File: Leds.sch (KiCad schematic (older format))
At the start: 140 parts

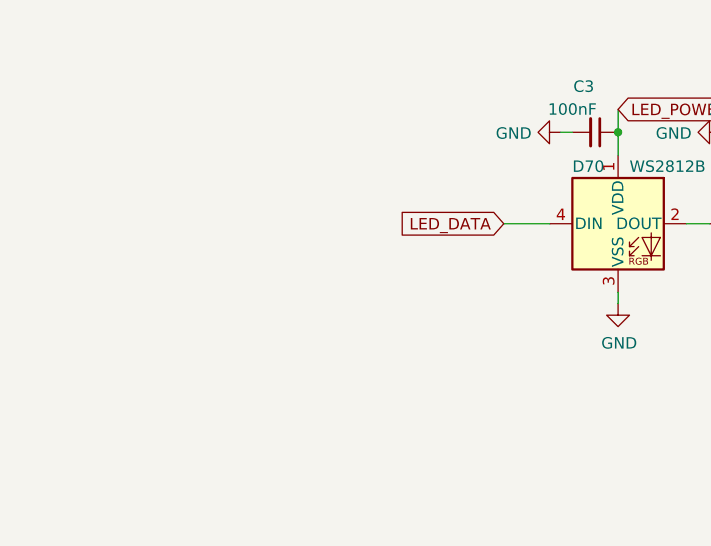
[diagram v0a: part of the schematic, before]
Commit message: add level shifter for ws2812
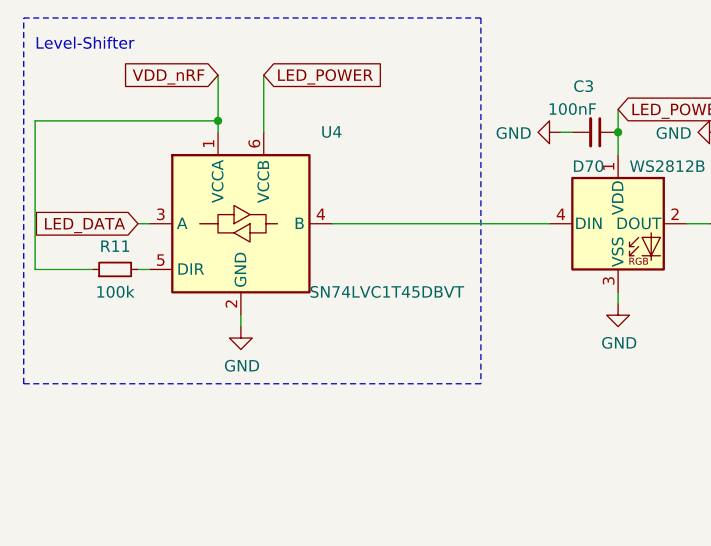
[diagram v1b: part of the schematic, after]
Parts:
- added R11: 100k, Resistor_SMD:R_0805_2012Metric, symbol Device:R_Small
- added U4: SN74LVC1T45DBVT, Package_TO_SOT_SMD:SOT-23-6, symbol Logic_LevelTranslator:SN74LVC1T45DBV
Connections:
- net GND: now also U4.2 (GND)
- net LED_DATA: now also U4.3 (A); no longer D70.4 (DIN)
- net LED_POWER: now also U4.6 (VCCB)
- new net: D70.4 (DIN), U4.4 (B)
- new net: R11.2, U4.5 (DIR)
- new net VDD_nRF: R11.1, U4.1 (VCCA)
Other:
- note added: "Level-Shifter"
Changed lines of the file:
@@
 Comment4 ""
 $EndDescr
-Text GLabel 3550 1400 0    50   Input ~ 0
+Text GLabel 1950 1400 0    50   Input ~ 0
 LED_DATA
 $Comp
@@
 Wire Wire Line
 	4350 1400 4450 1400
-Wire Wire Line
-	3550 1400 3750 1400
 $Comp
 L LED:WS2812B D70
@@
 $EndComp
 Connection ~ 9050 8150
+$Comp
+L Logic_LevelTranslator:SN74LVC1T45DBV U4
+U 1 1 5F93B2C8
+P 2400 1400
+F 0 "U4" H 2750 1800 50  0000 L CNN
+F 1 "SN74LVC1T45DBVT" H 2700 1100 50  0000 L CNN
+F 2 "Package_TO_SOT_SMD:SOT-23-6" H 2400 950 50  0001 C CNN
+F 3 "https://datasheet.lcsc.com/szlcsc/Texas-Instruments-TI-SN74LVC1T45DBVT_C116653.pdf" H 1500 750 50  0001 C CNN
+	1    2400 1400
+	1    0    0    -1
+$EndComp
+$Comp
+L Device:R_Small R11
+U 1 1 5F946E06
+P 1850 1600
+F 0 "R11" V 1950 1600 50  0000 C CNN
+F 1 "100k" V 1750 1600 50  0000 C CNN
+F 2 "Resistor_SMD:R_0805_2012Metric" H 1850 1600 50  0001 C CNN
+F 3 "~" H 1850 1600 50  0001 C CNN
+	1    1850 1600
+	0    -1   -1   0
+$EndComp
+$Comp
+L power:GND #PWR0160
+U 1 1 5F947445
+P 2400 1850
+F 0 "#PWR0160" H 2400 1600 50  0001 C CNN
+F 1 "GND" H 2405 1677 50  0000 C CNN
+F 2 "" H 2400 1850 50  0001 C CNN
+F 3 "" H 2400 1850 50  0001 C CNN
+	1    2400 1850
+	1    0    0    -1
+$EndComp
+Text GLabel 2500 750  2    50   Input ~ 0
+LED_POWER
+Text GLabel 2300 750  0    50   Input ~ 0
+VDD_nRF
+Wire Wire Line
+	1950 1600 2000 1600
+Wire Wire Line
+	2400 1800 2400 1850
+Wire Wire Line
+	1950 1400 2000 1400
+Wire Wire Line
+	2500 750  2500 1000
+Wire Wire Line
+	2300 750  2300 950
+Wire Wire Line
+	1750 1600 1500 1600
+Wire Wire Line
+	1500 1600 1500 950
+Wire Wire Line
+	1500 950  2300 950
+Connection ~ 2300 950
+Wire Wire Line
+	2300 950  2300 1000
+Wire Wire Line
+	2800 1400 3750 1400
+Text Notes 1500 650  0    50   ~ 0
+Level-Shifter
+Wire Notes Line
+	3450 500  3450 2100
+Wire Notes Line
+	3450 2100 1450 2100
+Wire Notes Line
+	1450 2100 1450 500
+Wire Notes Line
+	1450 500  3450 500
 $EndSCHEMATC
